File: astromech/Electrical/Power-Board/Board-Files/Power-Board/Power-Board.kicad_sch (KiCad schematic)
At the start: 66 parts, among them Q1 Q_NMOS_DSG

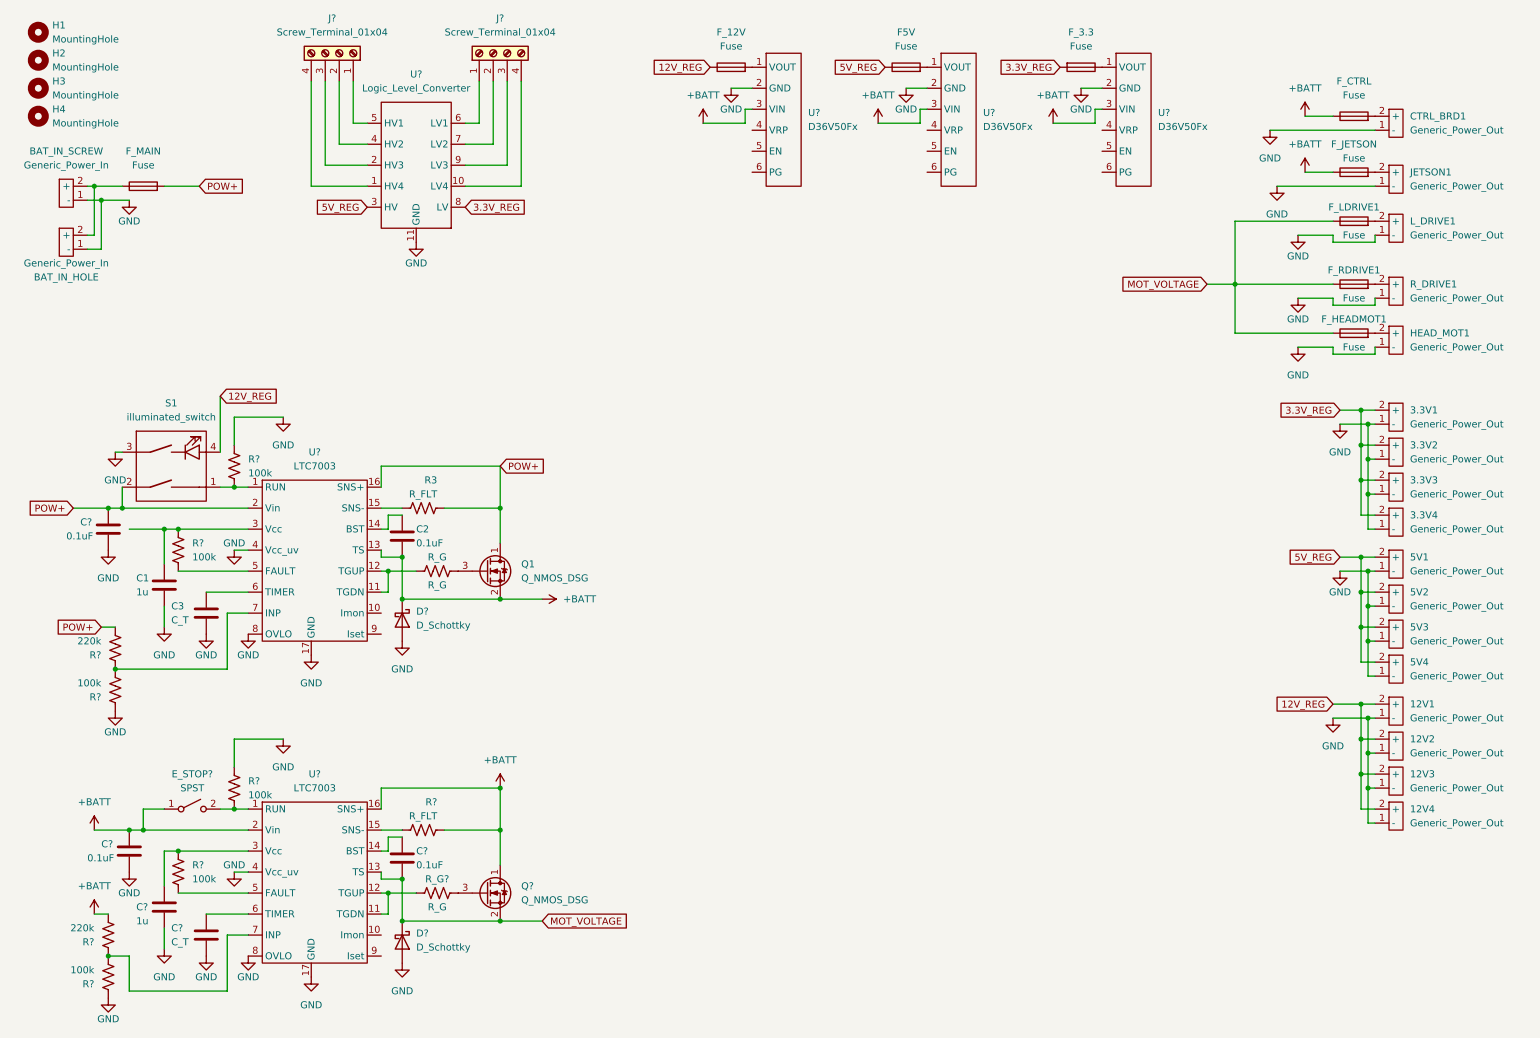
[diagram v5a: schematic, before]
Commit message: Renamed symbols in schematic
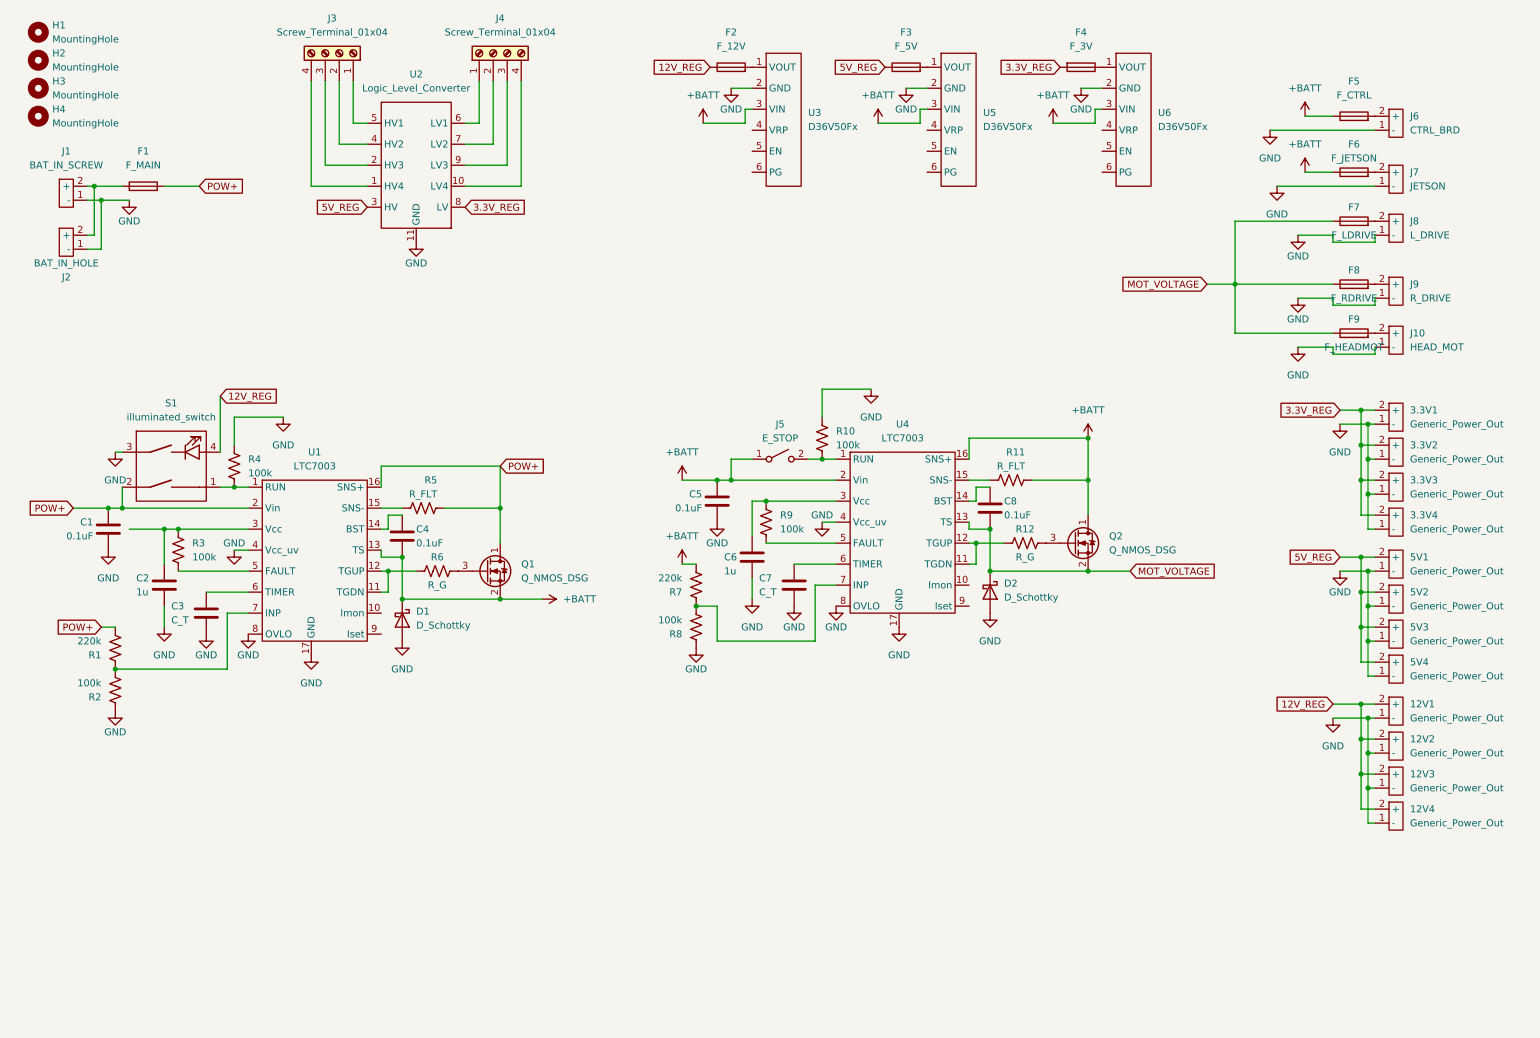
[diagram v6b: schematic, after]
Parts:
- F1: renamed from F_MAIN; value Fuse -> F_MAIN
- F2: renamed from F_12V; value Fuse -> F_12V
- F3: renamed from F5V; value Fuse -> F_5V
- F4: renamed from F_3.3; value Fuse -> F_3V
- F5: renamed from F_CTRL; value Fuse -> F_CTRL
- F6: renamed from F_JETSON; value Fuse -> F_JETSON
- F7: renamed from F_LDRIVE1; value Fuse -> F_LDRIVE
- F8: renamed from F_RDRIVE1; value Fuse -> F_RDRIVE
- F9: renamed from F_HEADMOT1; value Fuse -> F_HEADMOT
- J1: renamed from BAT_IN_SCREW; value Generic_Power_In -> BAT_IN_SCREW
- J10: renamed from HEAD_MOT1; value Generic_Power_Out -> HEAD_MOT
- J2: renamed from BAT_IN_HOLE; value Generic_Power_In -> BAT_IN_HOLE
- J5: renamed from E_STOP?; value SPST -> E_STOP
- J6: renamed from CTRL_BRD1; value Generic_Power_Out -> CTRL_BRD
- J7: renamed from JETSON1; value Generic_Power_Out -> JETSON
- J8: renamed from L_DRIVE1; value Generic_Power_Out -> L_DRIVE
- J9: renamed from R_DRIVE1; value Generic_Power_Out -> R_DRIVE
- gave numbers to parts that had none: 26
- renumbered C1 to C2, C2 to C4, R3 to R5, R_G to R6
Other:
- moved on the sheet: C5, C6, C7, C8, D2, J5, Q2, R10, R11, R12, R7, R8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

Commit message: Added grounded connections to level shifter
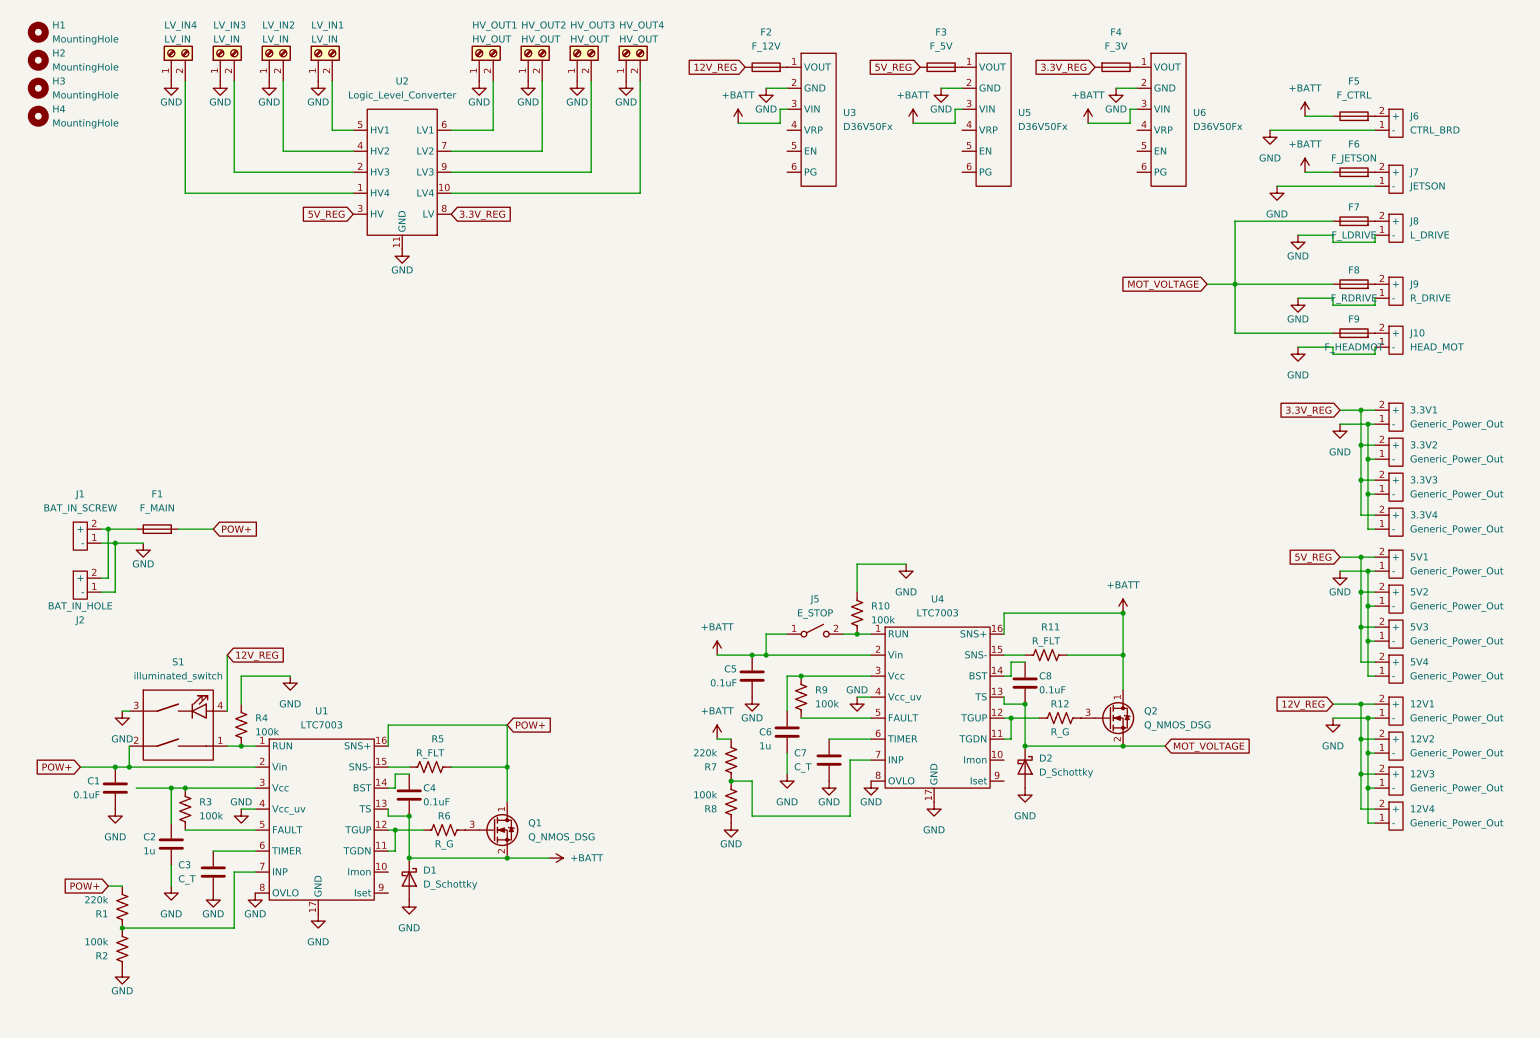
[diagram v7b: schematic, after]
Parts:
- removed J3, J4: Screw_Terminal_01x04, symbol Connector:Screw_Terminal_01x04
- added HV_OUT1, HV_OUT2, HV_OUT3, HV_OUT4: HV_OUT, symbol Connector:Screw_Terminal_01x02
- added LV_IN1, LV_IN2, LV_IN3, LV_IN4: LV_IN, symbol Connector:Screw_Terminal_01x02
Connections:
- net GND: now also HV_OUT1.1 (Pin_1), HV_OUT2.1 (Pin_1), HV_OUT3.1 (Pin_1), HV_OUT4.1 (Pin_1), LV_IN1.1 (Pin_1), LV_IN2.1 (Pin_1), LV_IN3.1 (Pin_1), LV_IN4.1 (Pin_1)
- net at U2.1 (HV4): now also LV_IN4.2 (Pin_2)
- net at U2.10 (LV4): now also HV_OUT4.2 (Pin_2)
- net at U2.2 (HV3): now also LV_IN3.2 (Pin_2)
- net at U2.4 (HV2): now also LV_IN2.2 (Pin_2)
- net at U2.5 (HV1): now also LV_IN1.2 (Pin_2)
- net at U2.6 (LV1): now also HV_OUT1.2 (Pin_2)
- net at U2.7 (LV2): now also HV_OUT2.2 (Pin_2)
- net at U2.9 (LV3): now also HV_OUT3.2 (Pin_2)
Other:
- moved on the sheet: C1, C2, C3, C4, C5, C6, C7, C8, D1, D2, F1, F2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

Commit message: added test points
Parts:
- added TP1, TP2: TestPoint, symbol Connector:TestPoint
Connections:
- net at R12.1, U4.11 (TGDN), U4.12 (TGUP): now also TP2.1
- net at R6.1, U1.11 (TGDN), U1.12 (TGUP): now also TP1.1
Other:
- moved on the sheet: C4, C8, D1, D2, Q1, Q2, R11, R12, R5, R6
